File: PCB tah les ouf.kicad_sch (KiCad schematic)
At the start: 19 parts, among them J1 USB_C_Receptacle_USB2.0_16P, U1 ESP32-S3-WROOM-1, U2 TMC2209_SILENTSTEPSTICK, U3 TMC2209_SILENTSTEPSTICK, U4 TMC2209_SILENTSTEPSTICK, U5 TMC2209_SILENTSTEPSTICK, U6 D3V3XA4B10LP, U7 AMS1117-3.3

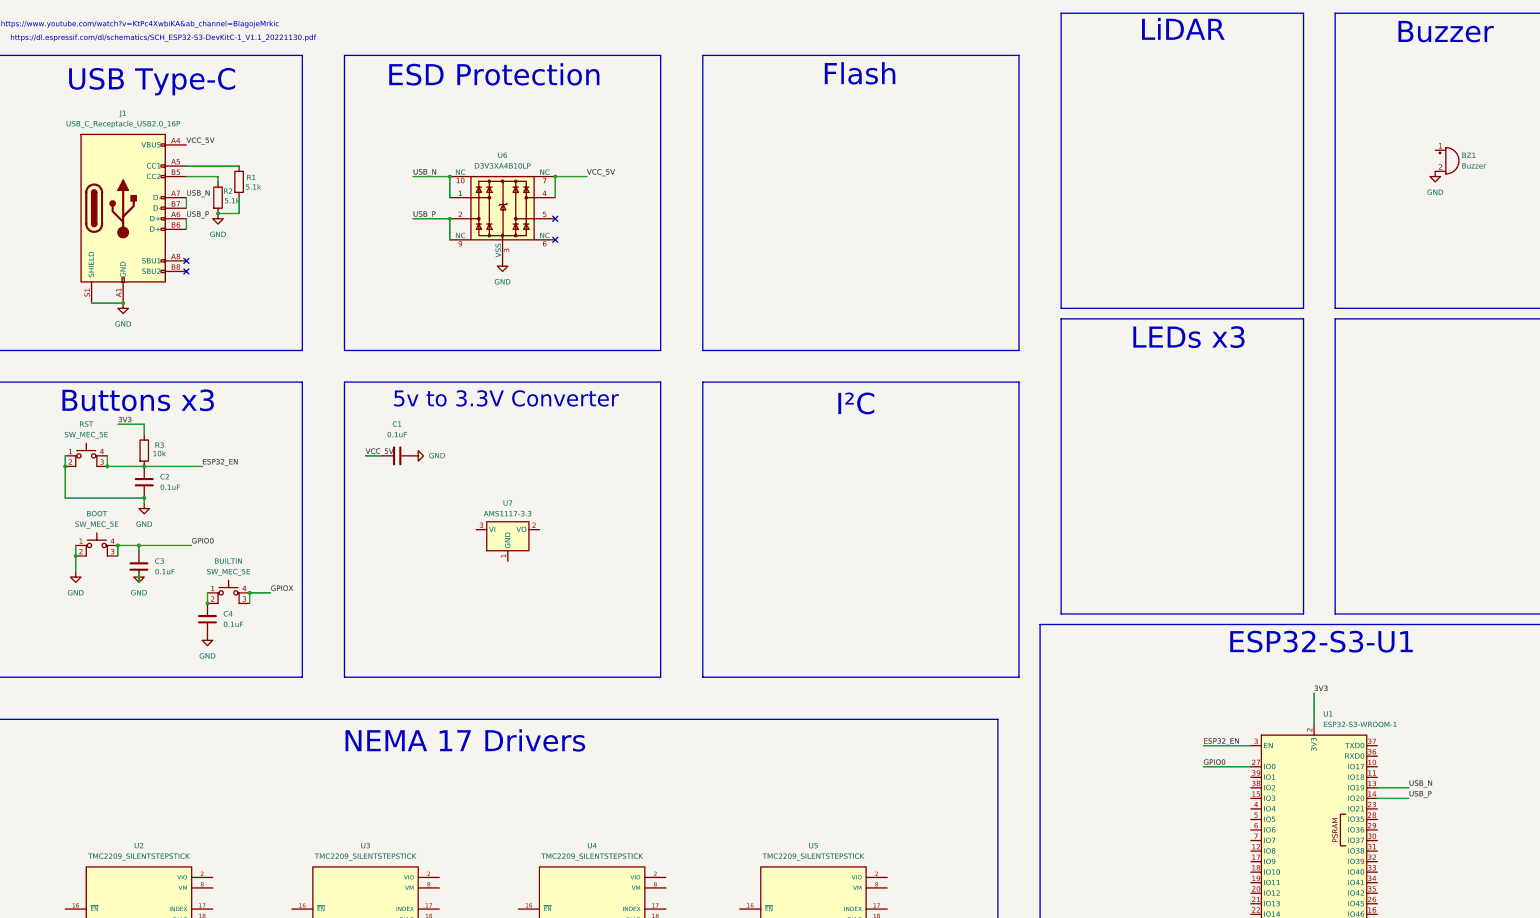
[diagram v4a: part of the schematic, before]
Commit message: Ajout Auto flash mode
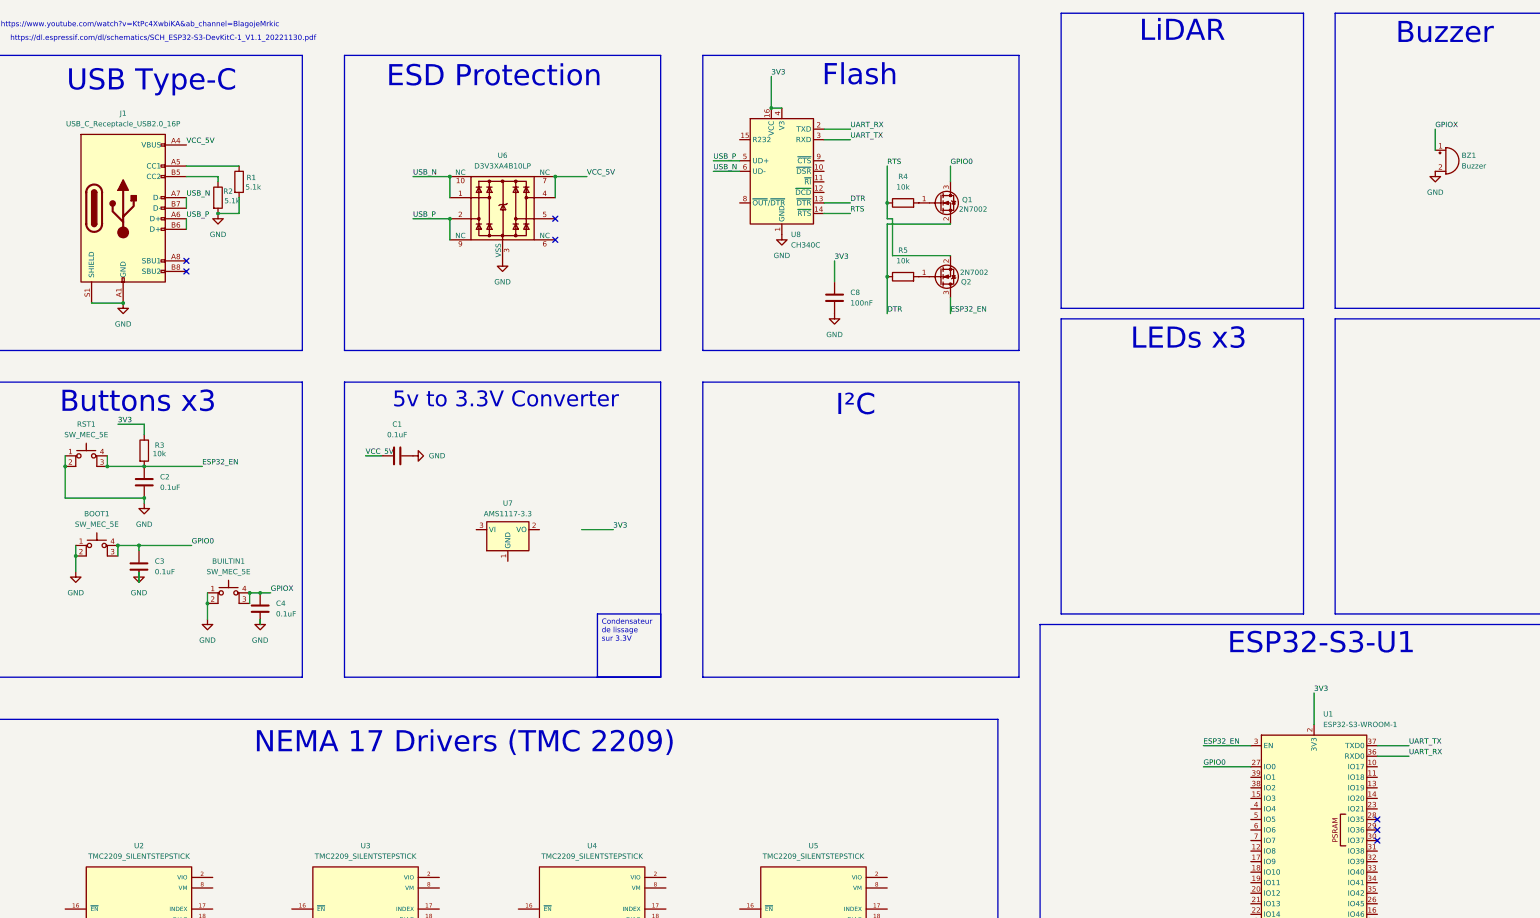
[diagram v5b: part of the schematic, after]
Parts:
- added C8: 100nF, symbol Device:C
- added Q1, Q2: 2N7002, Package_TO_SOT_SMD:SOT-23, symbol Transistor_FET:2N7002
- added R4, R5: 10k, symbol Device:R
- added U8: CH340C, Package_SO:SOIC-16_3.9x9.9mm_P1.27mm, symbol Interface_USB:CH340C
- renumbered BOOT to BOOT1, BUILTIN to BUILTIN1, RST to RST1
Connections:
- net 3V3: now also C8.1, U8.16 (VCC), U8.4 (V3)
- net ESP32_EN: now also Q2.3 (D)
- net GND: now also BUILTIN1.1, BUILTIN1.2, C8.2, U8.1 (GND)
- net GPIO0: now also Q1.3 (D)
- net GPIOX: now also BZ1.1 (+), C4.1
- net USB_N: now also U8.6 (UD-); no longer U1.13 (IO19)
- net USB_P: now also U8.5 (UD+); no longer U1.14 (IO20)
- net UART_RX: now reaches U1.36 (RXD0)
- net UART_RX: now also U8.2 (TXD)
- net UART_TX: now reaches U1.37 (TXD0)
- net UART_TX: now also U8.3 (RXD)
- new net: Q2.1 (G), R5.2
- new net: Q1.1 (G), R4.2
- new net DTR: Q1.2 (S), R5.1, U8.13 (~{DTR})
- new net RTS: Q2.2 (S), R4.1, U8.14 (~{RTS})
- no-connect marks 4 -> 7
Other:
- note added: "NEMA 17 Drivers (TMC 2209)"
- note removed: "NEMA 17 Drivers"
- moved on the sheet: C4

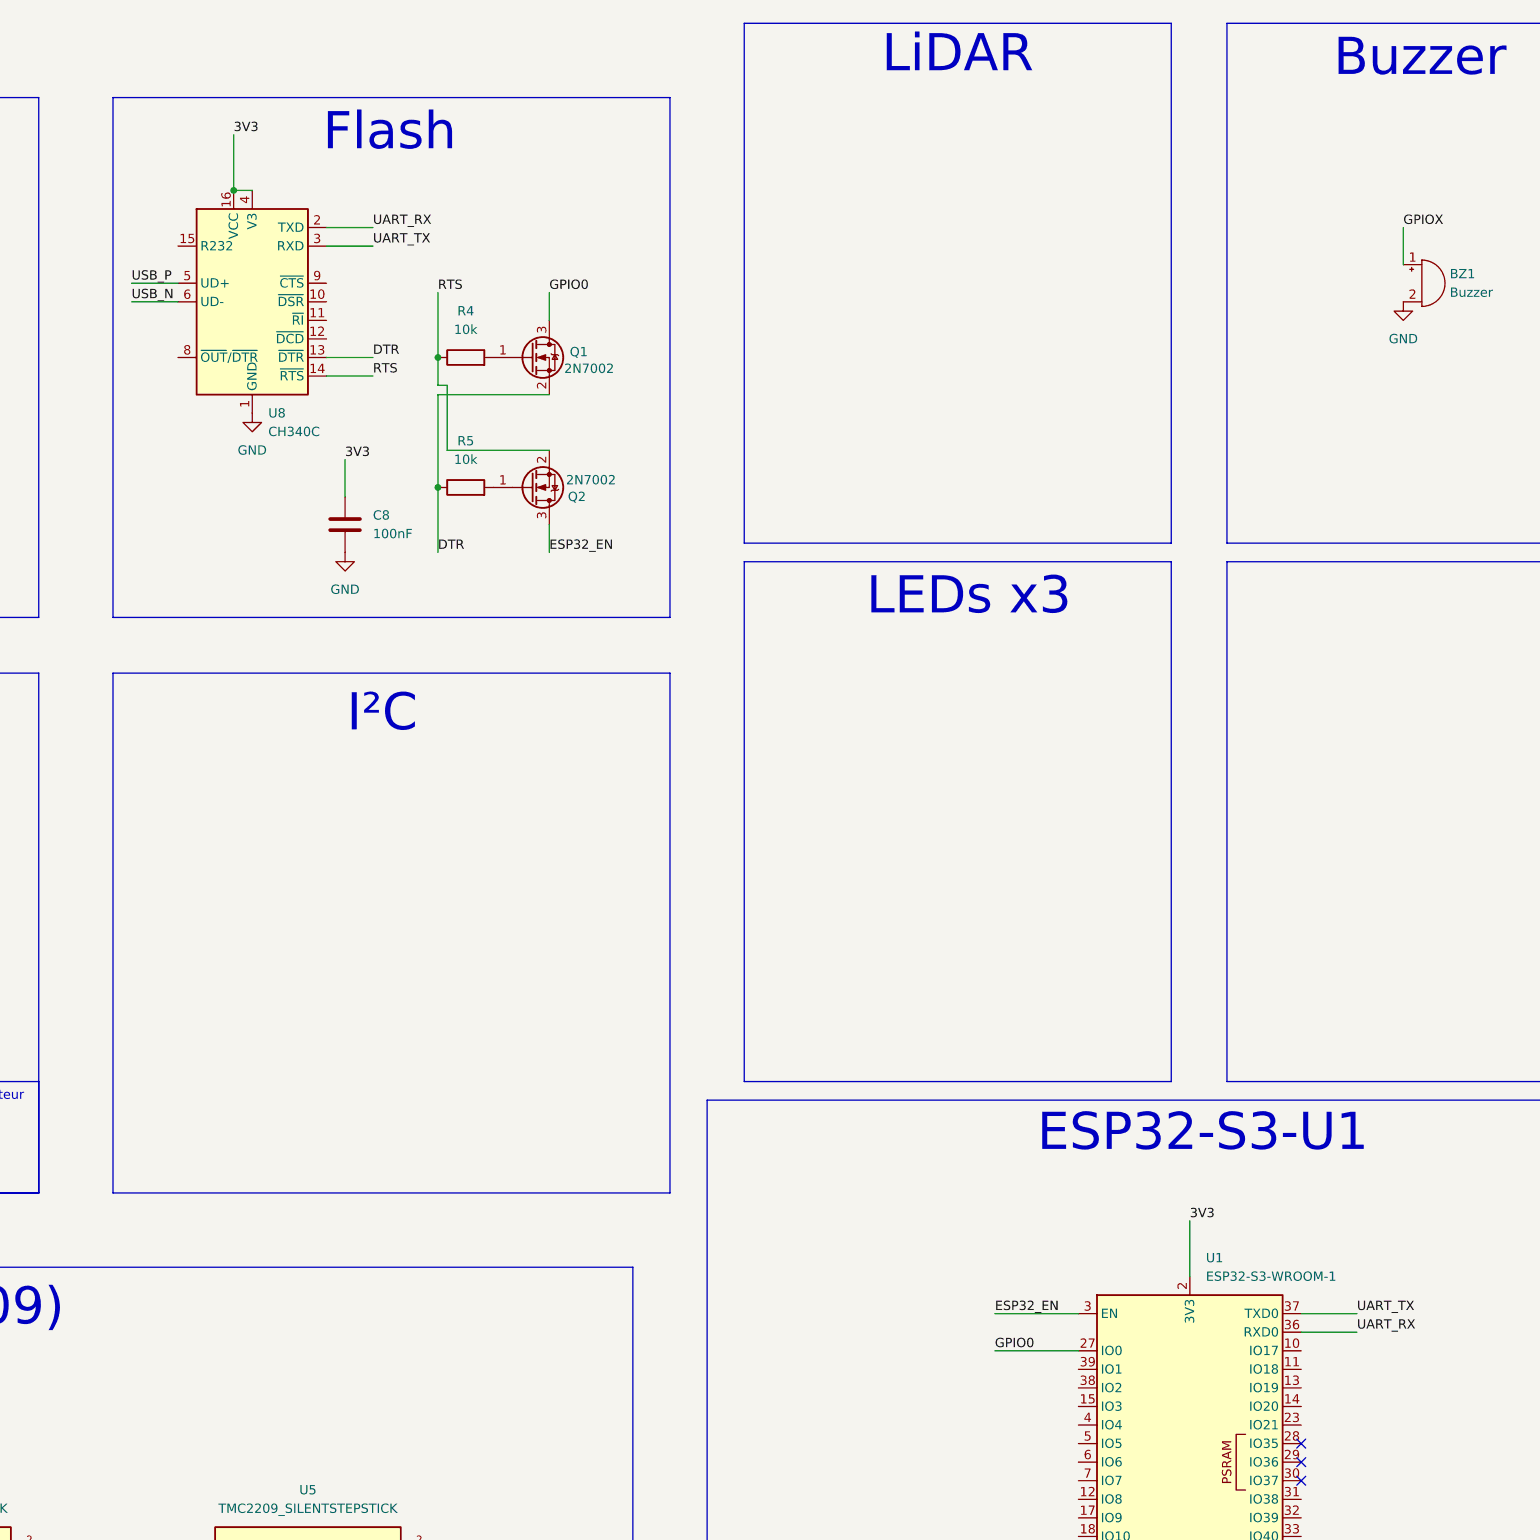
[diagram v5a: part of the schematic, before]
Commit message: auto flash mode v2
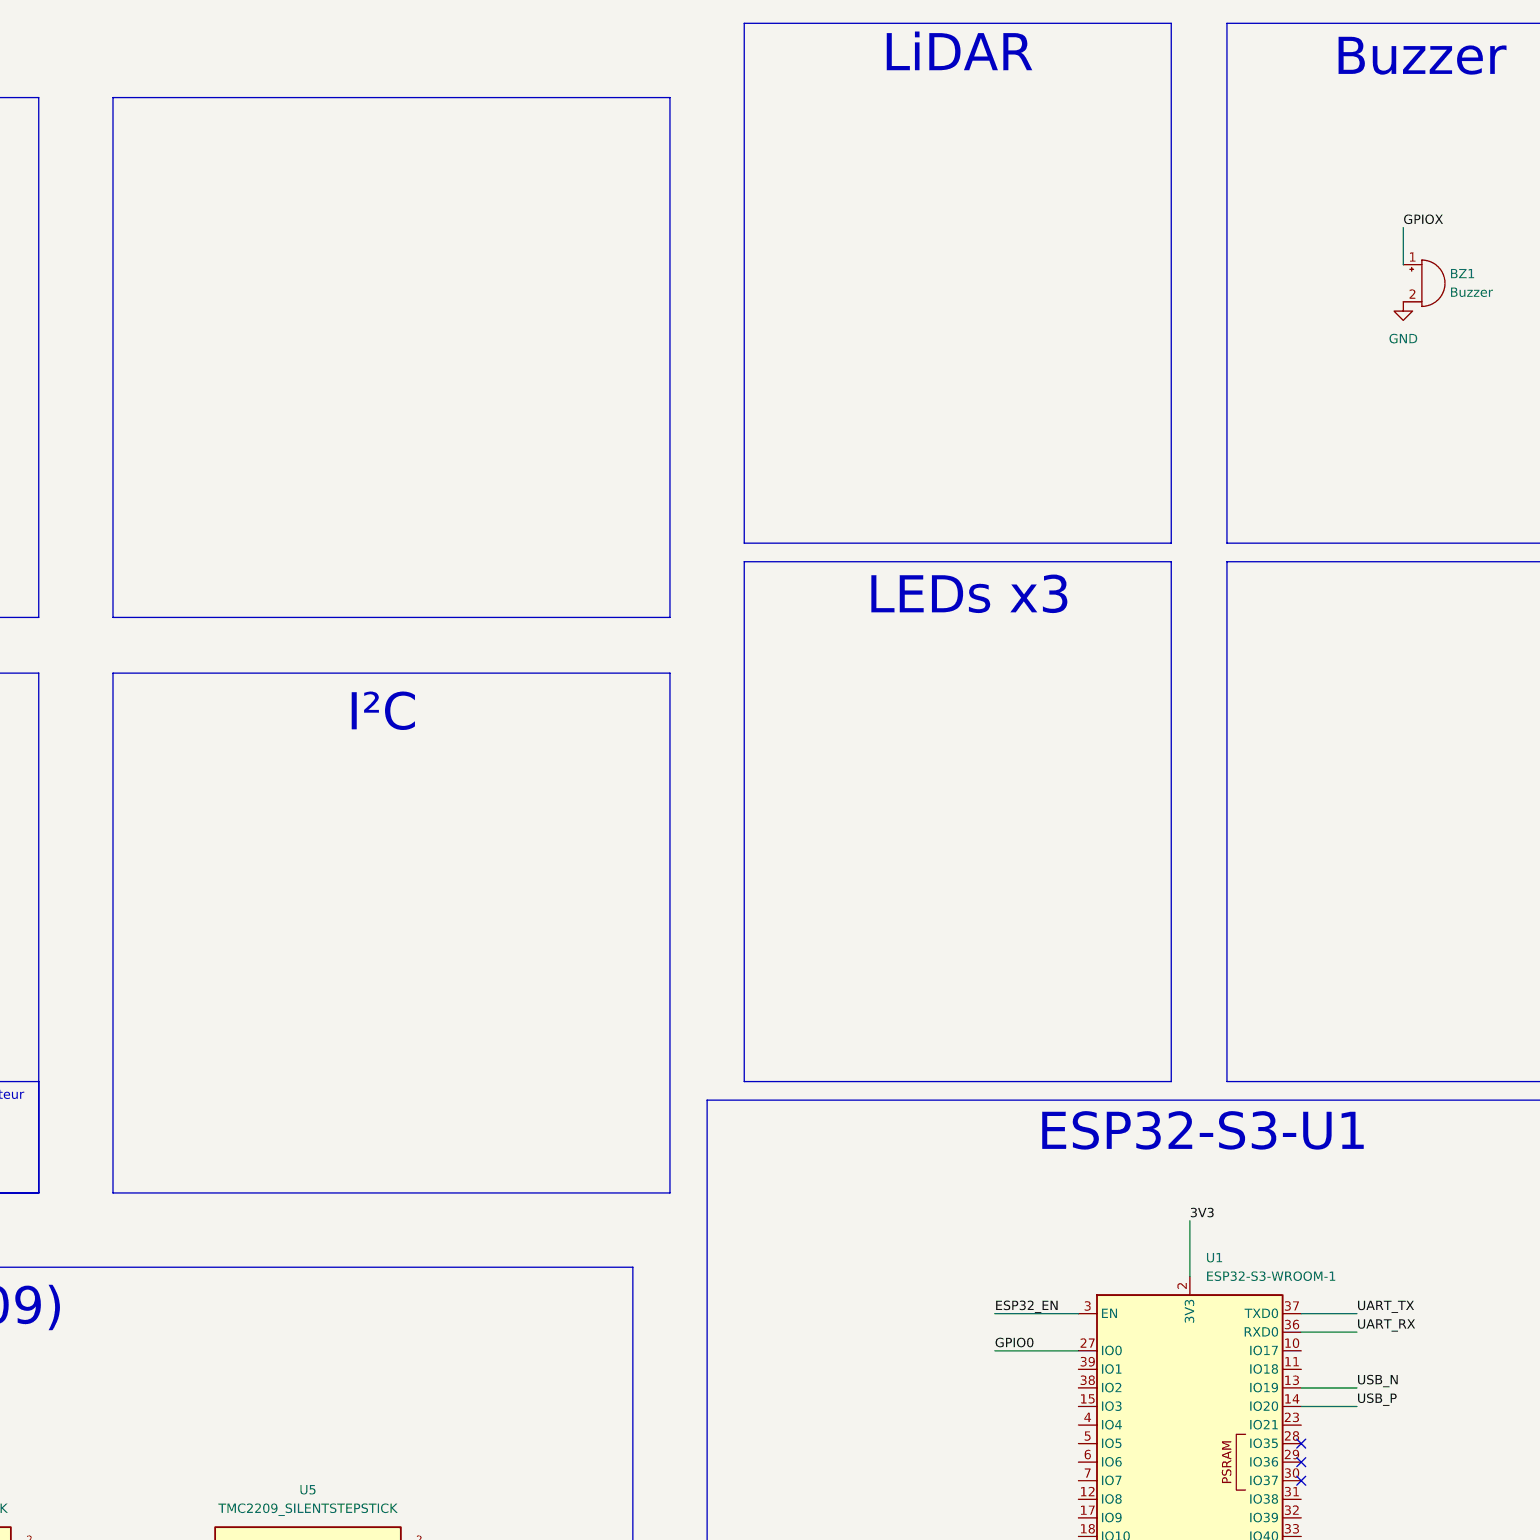
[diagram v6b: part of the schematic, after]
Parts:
- removed C8: 100nF, symbol Device:C
- removed Q1, Q2: 2N7002, Package_TO_SOT_SMD:SOT-23, symbol Transistor_FET:2N7002
- removed R4, R5: 10k, symbol Device:R
- removed U8: CH340C, Package_SO:SOIC-16_3.9x9.9mm_P1.27mm, symbol Interface_USB:CH340C
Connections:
- net USB_N: now also U1.13 (IO19)
- net USB_P: now also U1.14 (IO20)
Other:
- note removed: "Flash"
